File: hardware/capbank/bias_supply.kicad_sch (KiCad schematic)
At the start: 33 parts, among them U12 LM317AEMP, U13 74HC14, U14 MCP1415, U15 MCP1415

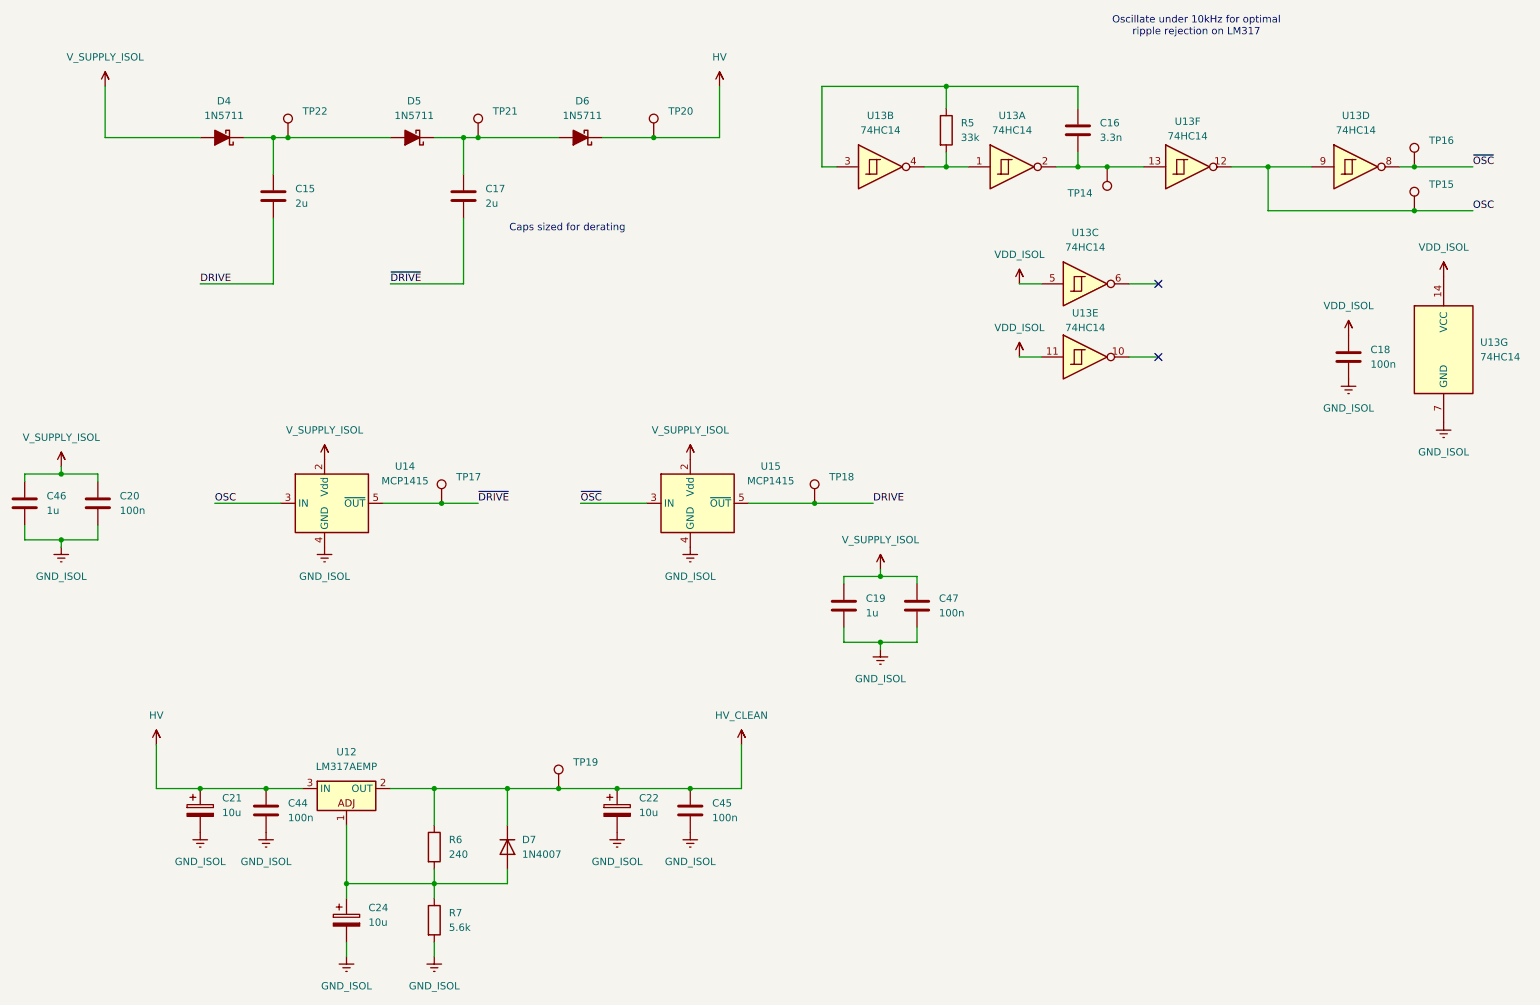
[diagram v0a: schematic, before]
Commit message: Progress, layout nearly completed, build oscillator on breadboard
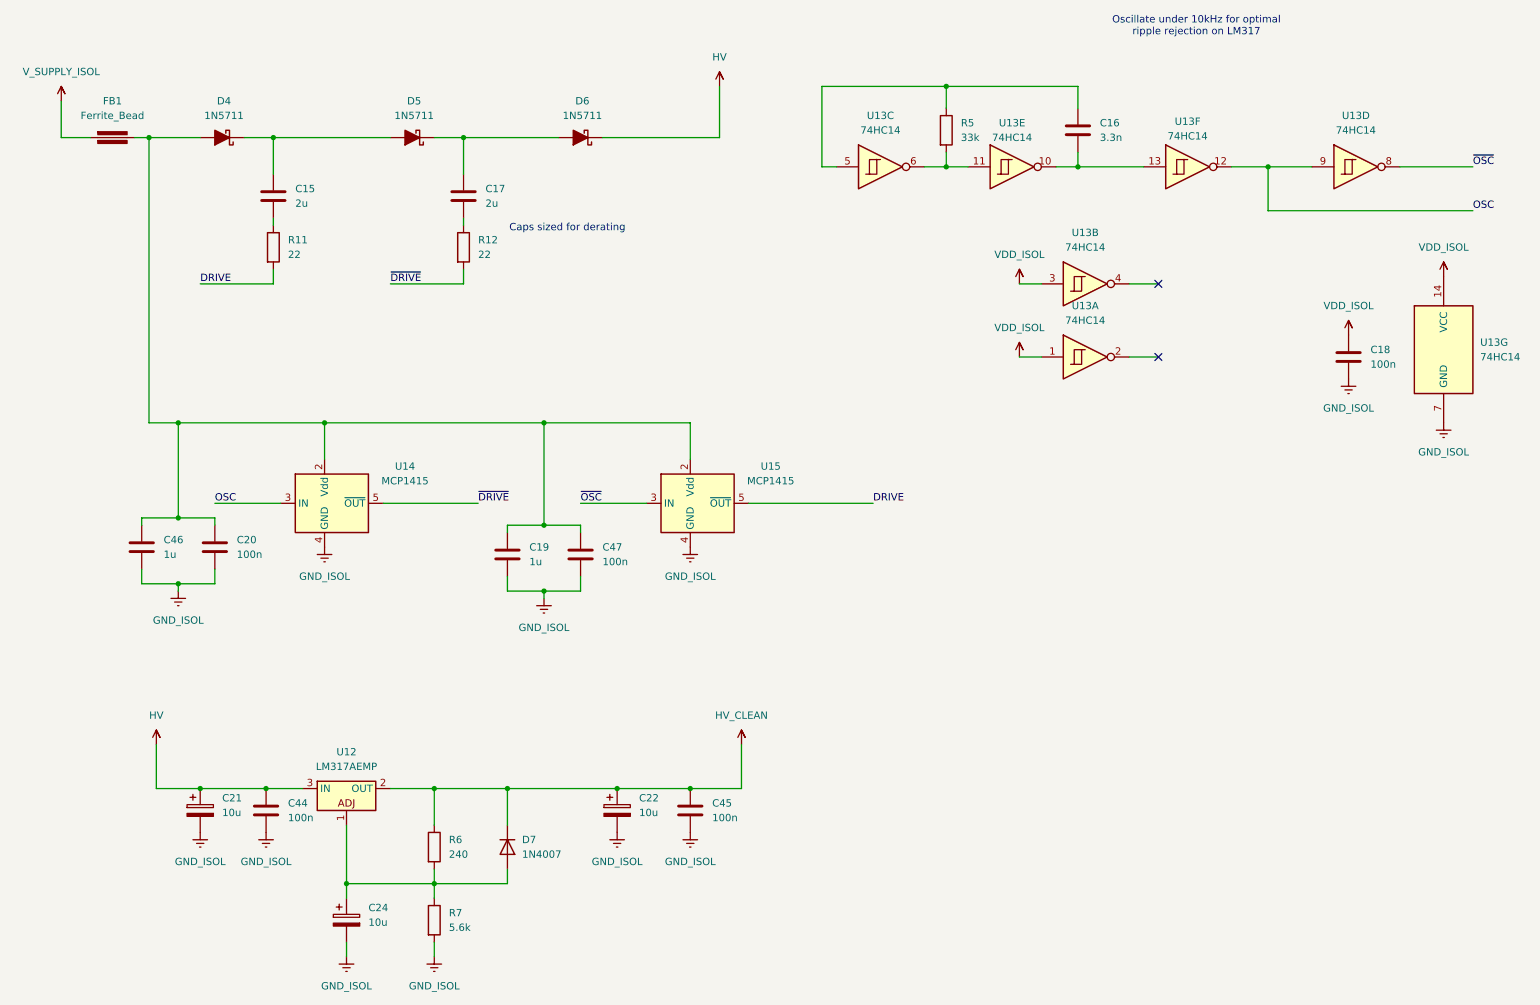
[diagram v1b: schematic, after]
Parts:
- removed TP14, TP15, TP16, TP17, TP18, TP19, TP20, TP21, TP22: ~, TestPoint:TestPoint_THTPad_1.5x1.5mm_Drill0.7mm, symbol Connector:TestPoint
- added FB1: Ferrite_Bead, PCM_Ferrite_SMD_AKL:Ferrite_0603_1608Metric, symbol PCM_Device_AKL:Ferrite_Bead
- added R11, R12: 22, PCM_Resistor_SMD_AKL:R_0603_1608Metric, symbol Device:R
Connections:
- net DRIVE: now also R11.2; no longer C15.2
- net VDD_ISOL: now also U13.1, U13.3; no longer U13.11, U13.5
- net V_SUPPLY_ISOL: now also FB1.1; no longer C19.1, C20.1, C46.1, C47.1, D4.2 (A), U14.2 (Vdd), U15.2 (Vdd)
- net ~{DRIVE}: now also R12.2; no longer C17.2
- net at U13.6: now also R5.2, U13.11
- net at C16.2, U13.13: now also U13.10; no longer U13.2
- net at C16.1, R5.1: now also U13.5; no longer U13.3
- new net: C17.2, R12.1
- new net: C19.1, C20.1, C46.1, C47.1, D4.2 (A), FB1.2, U14.2 (Vdd), U15.2 (Vdd)
- new net: C15.2, R11.1
- now unconnected: U13.4
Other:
- moved on the sheet: C19, C20, C46, C47, U13A, U13B, U13C, U13E
